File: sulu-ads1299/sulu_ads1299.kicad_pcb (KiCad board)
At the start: 2 copper layers, 35.8 x 42.8 mm, 78 parts, among them J1 Conn_01x08, J11 through_hole, J16 through_hole, J2 Conn_01x02, J20 through_hole, J3 Conn_02x05_Odd_Even, J4 through_hole, J5 through_hole, J6 through_hole, J7 Conn_01x08, J8 through_hole, Q1 BSS138, Q2 BSS138, SW1 SW_DIP_x02, U1 TPS62222DDCT, U2 TPS62222DDCT, U3 LM2775DSG, U4 ADS1299_TQFP-64, U5 scum3

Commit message: DRC clean layout of Rev. 3
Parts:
- removed D5, D6: GDZ5V1LP3-7, Diode_SMD:D_0402_1005Metric
- removed J3: Conn_02x05_Odd_Even, Connector_PinSocket_2.54mm:PinSocket_2x05_P2.54mm_Vertical_SMD
- added C32: 0.01uF, Capacitor_SMD:C_0603_1608Metric, F.Cu at (96.1, 81.9)
- added J9: Conn_02x06_Odd_Even, Connector_PinHeader_2.54mm:PinHeader_2x06_P2.54mm_Vertical_SMD, F.Cu at (103.4, 90.4)
- added R15: 4.99K, Resistor_SMD:R_0603_1608Metric, F.Cu at (93.9, 86.0)
- added R16: 392K, Resistor_SMD:R_0603_1608Metric, F.Cu at (96.1, 83.6)
- added RZ1: 0 Ohm, Resistor_SMD:R_0402_1005Metric, F.Cu at (90.2, 70.0)
- added RZ2: NP, Resistor_SMD:R_0402_1005Metric, F.Cu at (90.2, 71.2)
- added TP4: TestPoint, SCUM:through_hole, F.Cu at (117.3, 83.7)
- TP1: moved to B.Cu
- moved J16 9.15 mm to (112.0, 61.7)
- moved J5 6.74 mm to (99.7, 51.9)
- moved C10 5.82 mm to (87.5, 71.5), turned to 0 degrees
- moved Q1 5.72 mm to (92.5, 93.1)
- moved J11 5.66 mm to (95.0, 55.9)
- moved C7 5.34 mm to (87.5, 70.0), turned to 0 degrees
- moved C15 5.21 mm to (95.2, 72.0), turned to 180 degrees
- moved J8 2.98 mm to (94.5, 54.6)
- moved D4 2.19 mm to (95.1, 79.9)
- moved D3 2.17 mm to (96.3, 79.9)
- moved D2 2.16 mm to (97.4, 79.9)
- moved J2 2.07 mm to (88.3, 84.9)
- moved TP1 1.71 mm to (111.8, 83.4), turned to 180 degrees
- moved C11 1.69 mm to (91.7, 79.7)
- moved C12 1.69 mm to (93.3, 78.9)
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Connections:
- C10 pad 2: /+1.8V_ADS -> /+1.8V_BACKUP
- L3 pad 1: /+1.8V_ADS -> /+1.8V_BACKUP
- U2 pad 4: /+1.8V_ADS -> /+1.8V_BACKUP
- U4 pad 61: unconnected-(U4-Pad61) -> /ADS1299/BIASINV
- U4 pad 63: unconnected-(U4-Pad63) -> /ADS1299/BIASOUT
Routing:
- net /SCUM_GPIO2: track 10.8 -> 48.7 mm, vias 0 -> 4
- net /SCUM_GPIO1: track 11.3 -> 48.6 mm, vias 0 -> 7
- net /SCUM_GPIO3: track 2.64 -> 26.7 mm, vias 0 -> 1
- net /SCUM_GPIO7: track 5.64 -> 27.4 mm, vias 0 -> 2
- net /SCUM_GPIO13: track 4.61 -> 24.3 mm, vias 2 -> 1
- net /SCUM_GPIO4: track 7.68 -> 26.9 mm
- net /+1.8V_ADS: track 51.8 -> 70.7 mm, vias 3 -> 4
- net /SCUM_GPIO14: track 4.05 -> 22.6 mm, vias 2 -> 1
- net /ADS_BIAS_ELEC: track 0.00 -> 17.5 mm, vias 0 -> 2
- net /SCUM_GPIO5: track 22.7 -> 37.9 mm, vias 2 -> 6
- net Net-(Q2-Pad2): track 0.00 -> 13.8 mm, vias 0 -> 2
- net /ADS1299/BIASOUT: track 0.00 -> 11.4 mm
- net /ADS1299/BIASINV: track 0.00 -> 9.21 mm
- net /+1.8V_BACKUP: track 0.00 -> 8.59 mm
- net /ADS_IN3N_CONN: track 3.00 -> 10.2 mm
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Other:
- board size 35.8 x 42.8 mm -> 36.3 x 46 mm

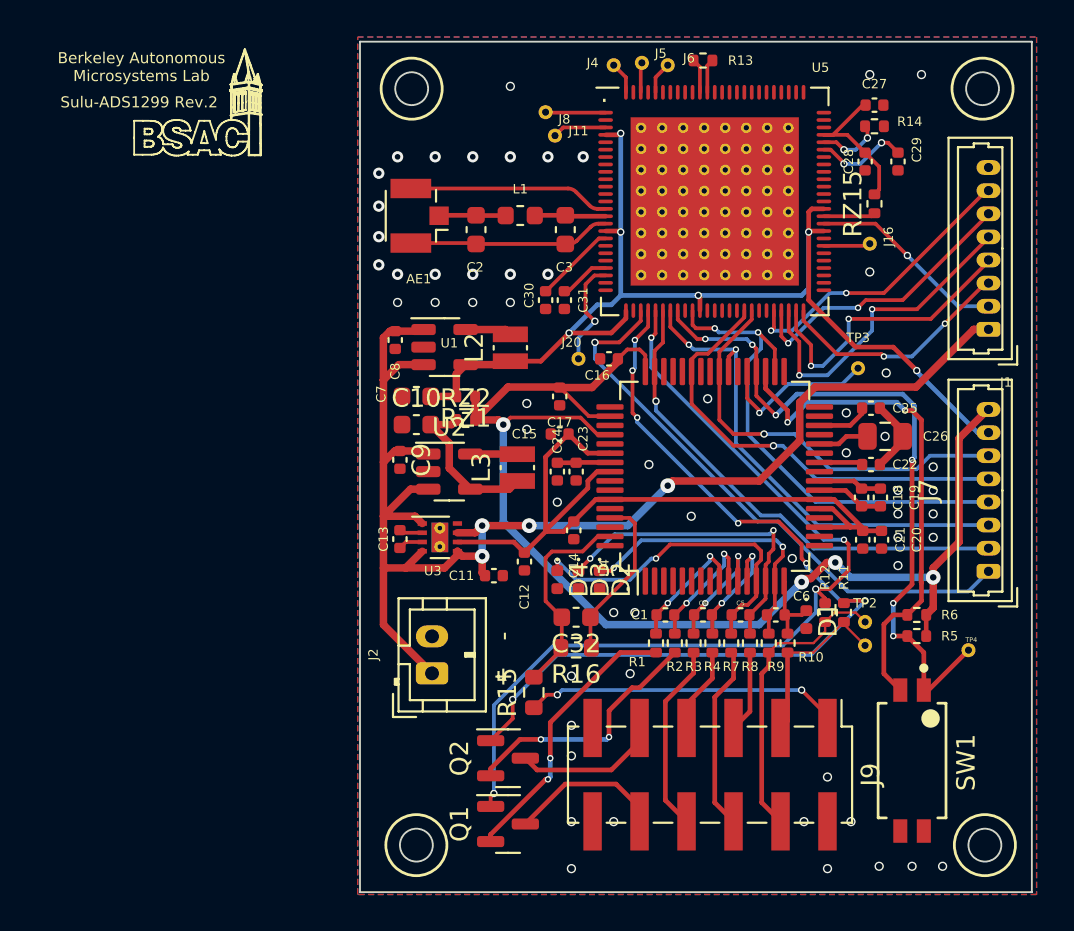
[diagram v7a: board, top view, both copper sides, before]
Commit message: Completed silkscreen for Rev. 3
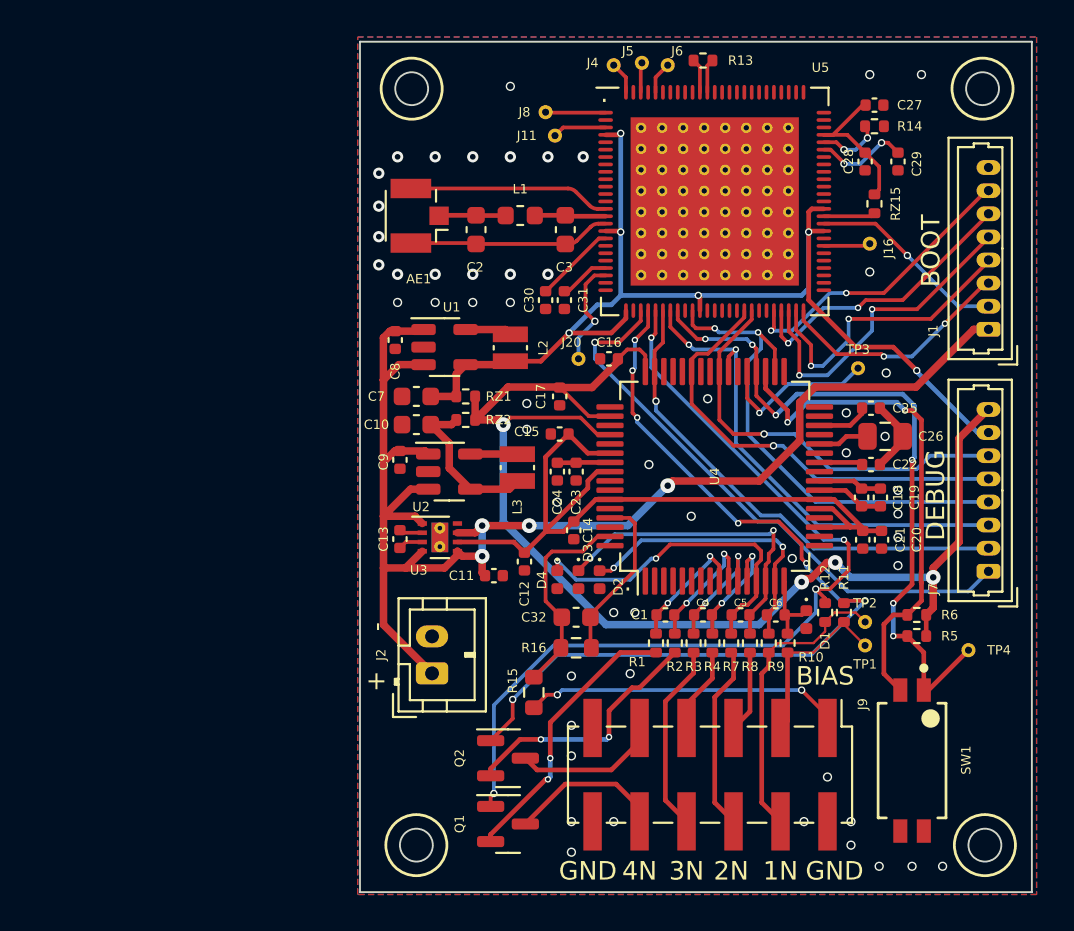
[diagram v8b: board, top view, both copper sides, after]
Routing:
- net GND: vias 58 -> 54
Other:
- board text added: "1N"
- board text added: "2N"
- board text added: "3N"
- board text added: "4N"
- board text added: "BIAS"
- board text added: "BOOT"
- board text added: "DEBUG"
- board text added: "GND"
- board text added: "Sulu-ADS1299 Rev.3"
- board text removed: "Sulu-ADS1299 Rev.2"
